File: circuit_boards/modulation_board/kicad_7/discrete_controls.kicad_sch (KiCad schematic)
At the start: 14 parts, among them SW11 E-Switch_EG2301

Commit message: Progress on circuit boards
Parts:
- removed D?: 1N4148W, Diode_SMD:D_SOD-123, symbol Diode:1N4148W
- removed Q?: MMBT3904, Package_TO_SOT_SMD:SOT-23, symbol Transistor_BJT:MMBT3904
- removed R?: 10k, symbol Device:R
- removed R?: 100k, symbol Device:R
- added C?: 100n, Capacitor_SMD:C_0603_1608Metric, symbol Device:C
- added R502, R503, R504: 100k, Resistor_SMD:R_0603_1608Metric, symbol Device:R
- added R505: 10k, Resistor_SMD:R_0603_1608Metric, symbol Device:R
- added R506, R507: 1M, Resistor_SMD:R_0603_1608Metric, symbol Device:R
- added SW11 (x7): E-Switch_EG2301B, custom_footprints:E-Switch_EG2301, symbol custom_symbols:E-Switch_EG2301
- added U803 (x2): MCP6002-xSN, Package_SO:SOIC-8_3.9x4.9mm_P1.27mm, symbol Amplifier_Operational:MCP6002-xSN
- R501: renamed from R?; value R -> 390; footprint (none) -> Resistor_SMD:R_0603_1608Metric
- SW11: value E-Switch_EG2301 -> E-Switch_EG2301B
- SW508: renamed from SW?; value ~ -> 5511M12; footprint (none) -> custom_footprints:E_Switch_5511M12
- gave numbers to parts that had none: 1
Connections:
- net +3.3V: now also C?.1
- net AUTO_GATE_LOGIC_A: now also SW11.1, U6.21 (I10); no longer SW11.1, U6.5 (I4)
- net AUTO_GATE_LOGIC_B: now also SW11.4, U6.20 (I11); no longer SW11.4, U6.4 (I5)
- net AUTO_GATE_SRC_A: now also SW11.1, U6.19 (I12); no longer SW11.1, U6.7 (I2)
- net AUTO_GATE_SRC_B: now also SW11.4, U6.18 (I13); no longer SW11.4, U6.6 (I3)
- net EXT_GATE: now also R502.2, R504.1
- net GND: now also C?.2, R502.1, R503.1, U803.3 (+), U803.3 (+)
- net MOD_ENV_TRIG_SRC_A: now also SW11.1, U6.4 (I5); no longer SW11.1, U6.23 (I8)
- net MOD_ENV_TRIG_SRC_B: now also SW11.4, U6.5 (I4); no longer SW11.4, U6.22 (I9)
- net PWM_LFO: now also R503.2, R505.1
- net PWM_LFO_SQR: now also R507.2, U803.1
- net S_AND_H_TRIG_SRC_A: now also SW11.1, U6.8 (I1); no longer SW11.1, U6.19 (I12)
- net S_AND_H_TRIG_SRC_B: now also SW11.4, U6.9 (I0); no longer SW11.4, U6.18 (I13)
- net VCA_ENV_TRIG_SRC_A: now also U6.23 (I8); no longer U6.21 (I10)
- net VCA_ENV_TRIG_SRC_B: now also U6.22 (I9); no longer U6.20 (I11)
- net VCF_ENV_TRIG_SRC_A: now also SW11.1, U6.6 (I3); no longer SW11.1, U6.3 (I6)
- net VCF_ENV_TRIG_SRC_B: now also SW11.4, U6.7 (I2); no longer SW11.4, U6.2 (I7)
- net ~{EXT_GATE}: now also R506.2, U803.1
- removed net RIBBON_MODE_A: SW11.1, U6.9 (I0)
- removed net RIBBON_MODE_B: SW11.4, U6.8 (I1)
- new net: R504.2, R506.1, U803.2 (-)
- new net: R505.2, R507.1, U803.2 (-)
- new net VCA_CTL_SRC_A: SW11.1, U6.2 (I7)
- new net VCA_CTL_SRC_B: SW11.4, U6.3 (I6)
- no-connect marks 9 -> 37
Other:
- note removed: "comparator goes here, output [0v, 3.3v]"

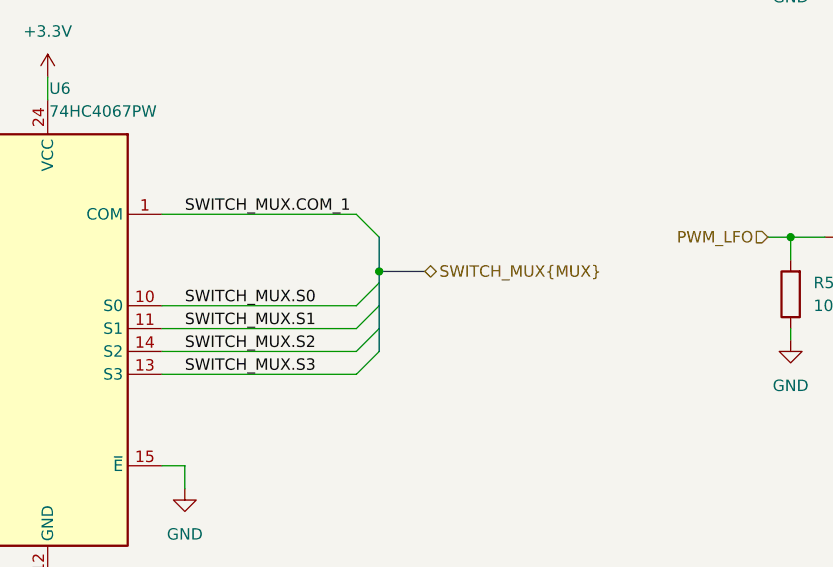
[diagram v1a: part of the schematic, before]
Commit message: Tweaks to mod board, add debug pin
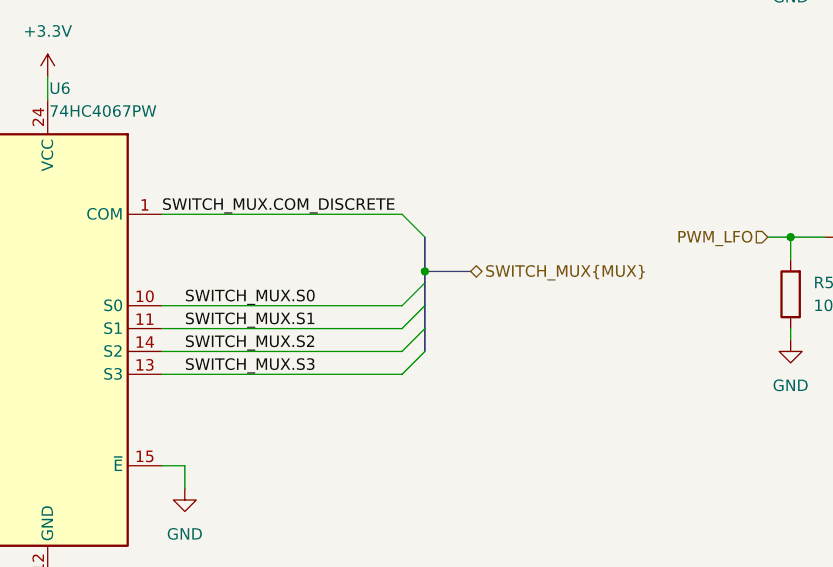
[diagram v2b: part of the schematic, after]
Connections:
- net SWITCH_MUX.COM_1 renamed SWITCH_MUX.COM_DISCRETE
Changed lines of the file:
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@@
   (junction (at 105.41 180.34) (diameter 0) (color 0 0 0 0)
   )
-  (junction (at 180.34 90.17) (diameter 0) (color 0 0 0 0)
+  (junction (at 185.42 90.17) (diameter 0) (color 0 0 0 0)
   )
   (no_connect (at 184.15 158.75))
@@
   (no_connect (at 260.35 161.29))
   (no_connect (at 276.86 156.21))
-  (bus_entry (at 180.34 91.44) (size -2.54 2.54)
-    (stroke (width 0) (type default))
-  )
-  (bus_entry (at 180.34 96.52) (size -2.54 2.54)
-    (stroke (width 0) (type default))
-  )
-  (bus_entry (at 180.34 93.98) (size -2.54 2.54)
-    (stroke (width 0) (type default))
-  )
-  (bus_entry (at 180.34 99.06) (size -2.54 2.54)
-    (stroke (width 0) (type default))
-  )
-  (bus_entry (at 177.8 83.82) (size 2.54 2.54)
+  (bus_entry (at 185.42 91.44) (size -2.54 2.54)
+    (stroke (width 0) (type default))
+  )
+  (bus_entry (at 185.42 96.52) (size -2.54 2.54)
+    (stroke (width 0) (type default))
+  )
+  (bus_entry (at 185.42 86.36) (size -2.54 -2.54)
+    (stroke (width 0) (type default))
+  )
+  (bus_entry (at 185.42 93.98) (size -2.54 2.54)
+    (stroke (width 0) (type default))
+  )
+  (bus_entry (at 185.42 99.06) (size -2.54 2.54)
     (stroke (width 0) (type default))
   )
@@
     (stroke (width 0) (type default))
   )
-  (bus (pts (xy 180.34 96.52) (xy 180.34 99.06))
+  (bus (pts (xy 185.42 96.52) (xy 185.42 99.06))
     (stroke (width 0) (type default))
   )
@@
     (stroke (width 0) (type default))
   )
-  (bus (pts (xy 180.34 86.36) (xy 180.34 90.17))
+  (bus (pts (xy 185.42 86.36) (xy 185.42 90.17))
     (stroke (width 0) (type default))
   )
@@
     (stroke (width 0) (type default))
   )
-  (wire (pts (xy 156.21 93.98) (xy 177.8 93.98))
+  (wire (pts (xy 156.21 93.98) (xy 182.88 93.98))
     (stroke (width 0) (type default))
   )
@@
     (stroke (width 0) (type default))
   )
-  (bus (pts (xy 180.34 93.98) (xy 180.34 96.52))
-    (stroke (width 0) (type default))
-  )
-  (wire (pts (xy 156.21 101.6) (xy 177.8 101.6))
+  (bus (pts (xy 185.42 93.98) (xy 185.42 96.52))
+    (stroke (width 0) (type default))
+  )
+  (wire (pts (xy 156.21 101.6) (xy 182.88 101.6))
     (stroke (width 0) (type default))
   )
@@
     (stroke (width 0) (type default))
   )
-  (bus (pts (xy 185.42 90.17) (xy 180.34 90.17))
+  (bus (pts (xy 190.5 90.17) (xy 185.42 90.17))
     (stroke (width 0) (type default))
   )
@@
     (stroke (width 0) (type default))
   )
-  (wire (pts (xy 156.21 83.82) (xy 177.8 83.82))
+  (wire (pts (xy 156.21 83.82) (xy 182.88 83.82))
     (stroke (width 0) (type default))
   )
@@
     (stroke (width 0) (type default))
   )
-  (wire (pts (xy 156.21 99.06) (xy 177.8 99.06))
+  (wire (pts (xy 156.21 99.06) (xy 182.88 99.06))
     (stroke (width 0) (type default))
   )
@@
     (stroke (width 0) (type default))
   )
-  (bus (pts (xy 180.34 90.17) (xy 180.34 91.44))
+  (bus (pts (xy 185.42 90.17) (xy 185.42 91.44))
     (stroke (width 0) (type default))
   )
@@
     (stroke (width 0) (type default))
   )
-  (wire (pts (xy 156.21 96.52) (xy 177.8 96.52))
+  (wire (pts (xy 156.21 96.52) (xy 182.88 96.52))
     (stroke (width 0) (type default))
   )
@@
     (stroke (width 0) (type default))
   )
-  (bus (pts (xy 180.34 91.44) (xy 180.34 93.98))
+  (bus (pts (xy 185.42 91.44) (xy 185.42 93.98))
     (stroke (width 0) (type default))
   )
@@
     (effects (font (size 1.27 1.27)) (justify left bottom))
   )
+  (label "SWITCH_MUX.COM_DISCRETE" (at 156.21 83.82 0) (fields_autoplaced)
+    (effects (font (size 1.27 1.27)) (justify left bottom))
+  )
   (label "MODOSC_ON_OFF_TOGGLE" (at 143.51 173.99 180) (fields_autoplaced)
     (effects (font (size 1.27 1.27)) (justify right bottom))
@@
   (label "S_AND_H_TRIG_SRC_A" (at 78.74 26.67 180) (fields_autoplaced)
     (effects (font (size 1.27 1.27)) (justify right bottom))
-  )
-  (label "SWITCH_MUX.COM_1" (at 158.75 83.82 0) (fields_autoplaced)
-    (effects (font (size 1.27 1.27)) (justify left bottom))
   )
   (label "S_AND_H_TRIG_SRC_B" (at 78.74 31.75 180) (fields_autoplaced)
@@
     (effects (font (size 1.27 1.27)) (justify right))
   )
-  (hierarchical_label "SWITCH_MUX{MUX}" (shape bidirectional) (at 185.42 90.17 0) (fields_autoplaced)
+  (hierarchical_label "SWITCH_MUX{MUX}" (shape bidirectional) (at 190.5 90.17 0) (fields_autoplaced)
     (effects (font (size 1.27 1.27)) (justify left))
   )
